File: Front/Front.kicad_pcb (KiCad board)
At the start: 2 copper layers, 40 x 40 mm, 43 parts, among them J1 USB_B_Micro, Q1 BC849, Q2 BC849, SW1 SW_DPDT_x2, U1 CH340C, U10 ESP32-WROOM-32, U2 CJVL53L0XV2, U3 SPX3819M5-L-3-3

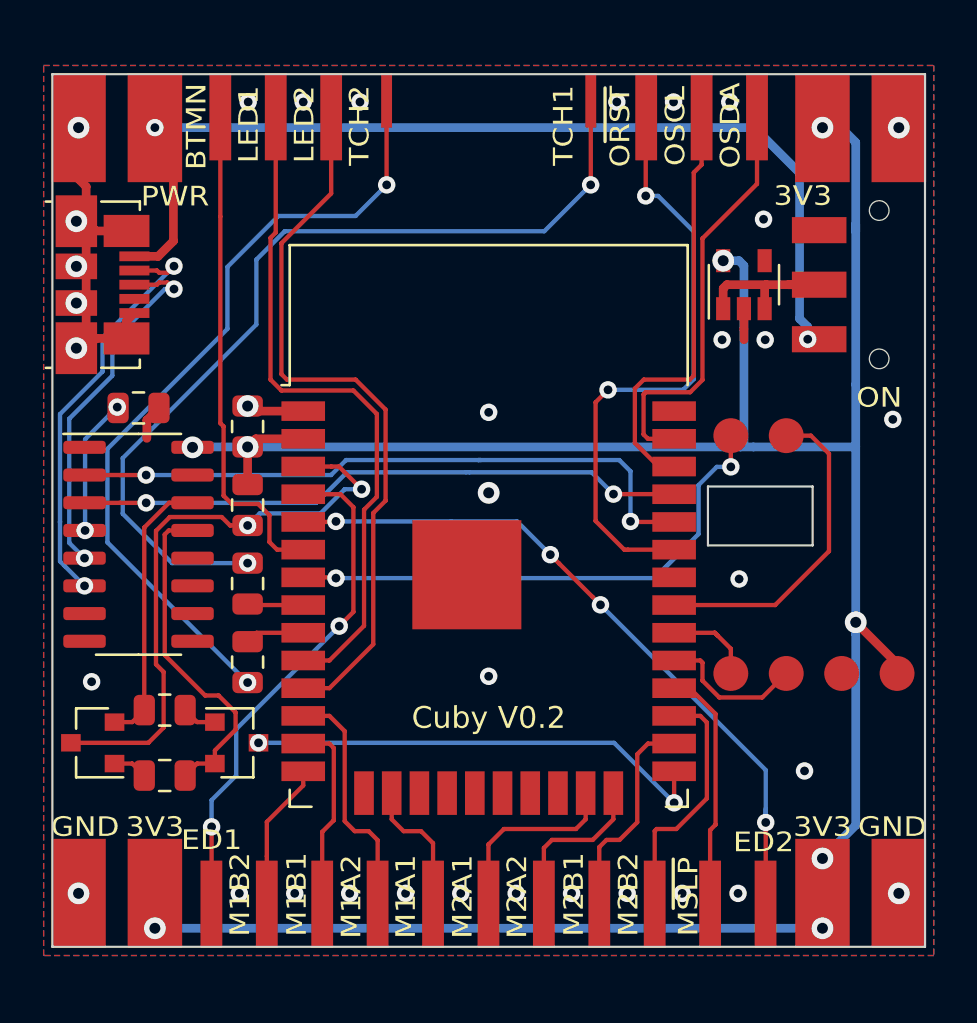
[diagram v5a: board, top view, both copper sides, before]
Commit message: removed extra pins in front, respaced pins in bottom and front
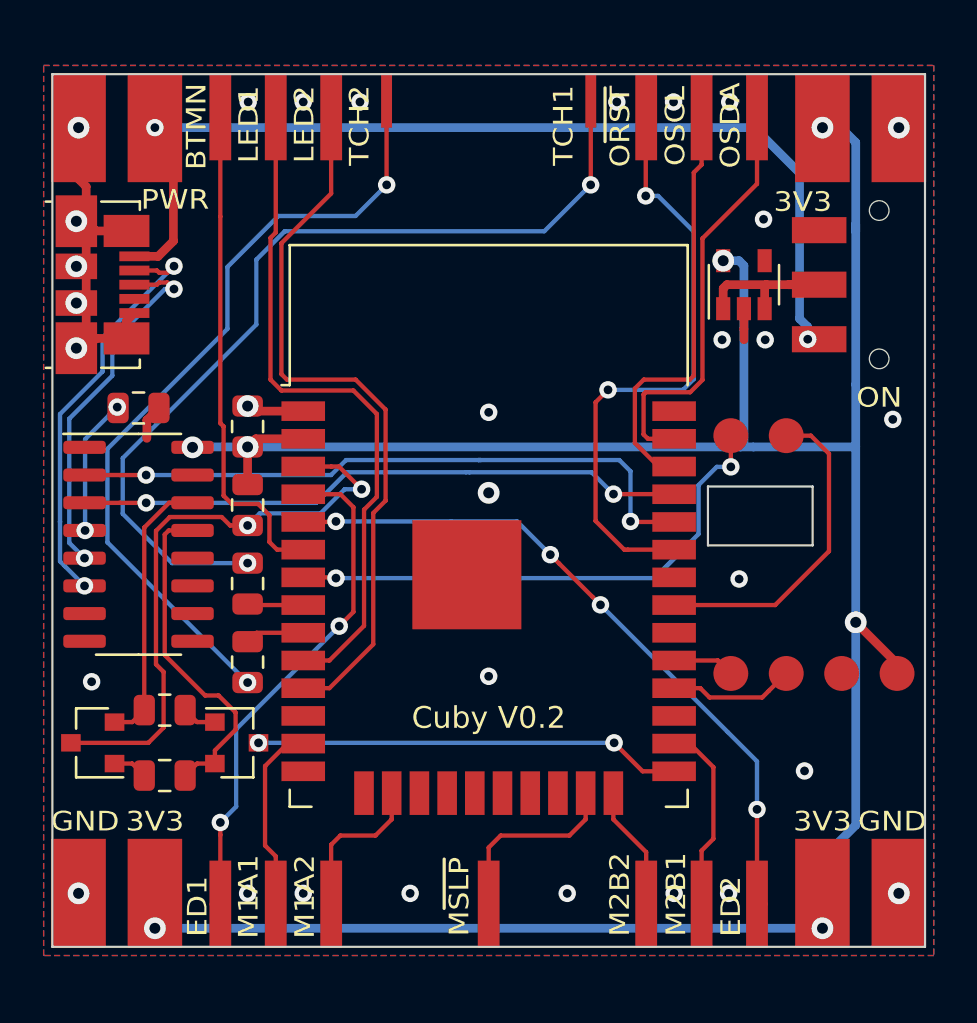
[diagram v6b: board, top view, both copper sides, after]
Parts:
- removed H3: M1B2, Custom:Mounting_Pad_Signal
- removed H4: M1B1, Custom:Mounting_Pad_Signal
- removed H7: M2A1, Custom:Mounting_Pad_Signal
- removed H8: M2A2, Custom:Mounting_Pad_Signal
- moved H2 10.2 mm to (215.5, 141.1)
- moved H6 7.21 mm to (205.7, 141.1)
- moved H9 4.69 mm to (225.3, 141.1)
- moved H5 2.13 mm to (208.3, 141.1)
- moved H12 0.41 mm to (203.2, 141.1)
- moved H10 0.39 mm to (222.7, 141.1)
- moved H13 0.39 mm to (227.8, 141.1)
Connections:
- U10 pad 12: /M1_AOUT2 -> (no net)
- U10 pad 13: /M1_BOUT1 -> /M1_AOUT1
- U10 pad 14: /M1_BOUT2 -> (no net)
- U10 pad 16: /M1_AOUT1 -> /M1_AOUT2
- U10 pad 23: /M2_AOUT1 -> /M1_M2_~SLEEP
- U10 pad 24: /M2_AOUT2 -> /M2_BOUT2
- U10 pad 27: /M2_BOUT2 -> (no net)
- U10 pad 28: /M1_M2_~SLEEP -> /OD_SCL
- U10 pad 29: /OD_SCL -> /OD_SDA
- U10 pad 30: /OD_SDA -> (no net)
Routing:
- net /M2_AOUT1: track 8.87 -> 0.00 mm
- net /M1_BOUT1: track 8.87 -> 0.00 mm
- net /M2_AOUT2: track 7.51 -> 0.00 mm
- net /M1_BOUT2: track 6.79 -> 0.00 mm
- net /M2_BOUT2: track 11.5 -> 5.72 mm
- net /M1_AOUT2: track 11.1 -> 7.19 mm
- net /M1_M2_~SLEEP: track 12.7 -> 8.78 mm
- net +3V3: track 113.6 -> 116.8 mm, vias 8 -> 7
- net /M1_AOUT1: track 6.35 -> 8.71 mm
- net /GPIO0: track 21.6 -> 19.6 mm
- net /ED_IN1: track 24.9 -> 23.3 mm
- net /OD_SDA: track 4.20 -> 2.85 mm
- net /OD_SCL: track 6.78 -> 5.77 mm
- net /ED_IN2: track 32.7 -> 31.9 mm
- net GND: vias 35 -> 31
